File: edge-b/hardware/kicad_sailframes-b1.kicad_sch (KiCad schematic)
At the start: 49 parts, among them J2 JST_PH_BAT, J3 U.FL, U1 LC29HEAMD, U2 TP4056, U3 MT3608

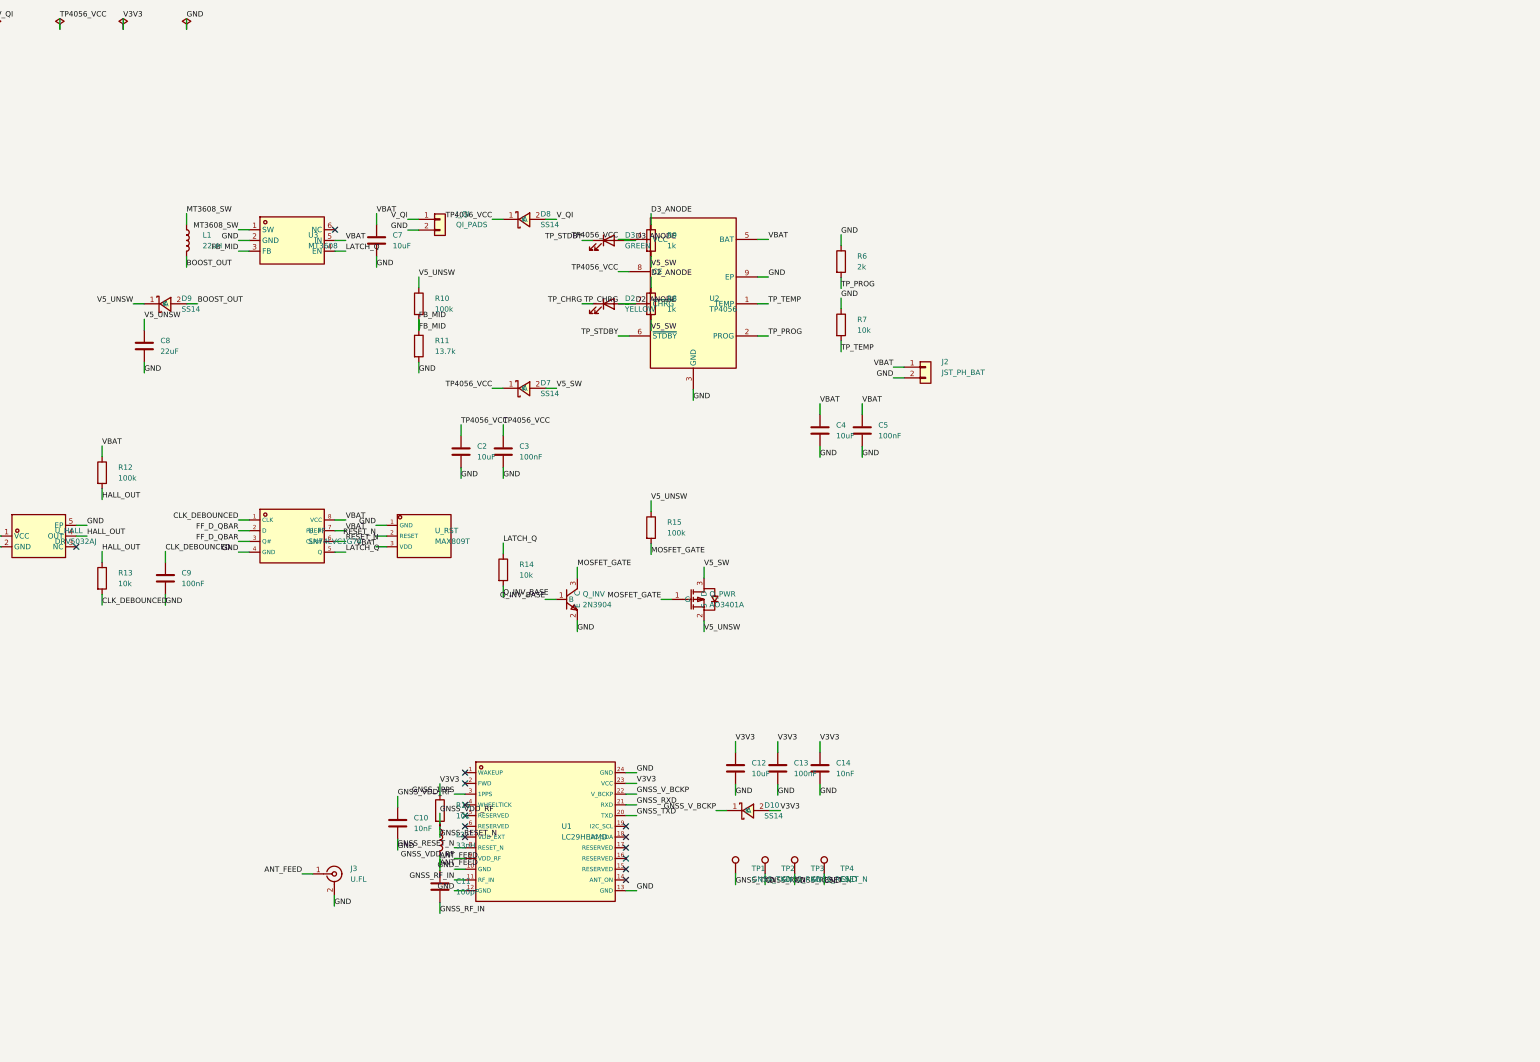
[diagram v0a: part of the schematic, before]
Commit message: B1 schematic Sections 4+5+6+7+9: ESP32, BNO085, TFT, microSD, LEDs
29 new components completing the schematic capture:
- Section 4: U4 ESP32 DevKit V1 socket (30-pin) with full GPIO mapping
  per B1_PIN_MAP.md. 6 pins marked no_connect (EN/VP/D12/D15/RX0/TX0 —
  reserved, strapping, or USB-handled).
- Section 5: J8 BNO085 9-pin socket + R21/R22 4.7K I2C pull-ups to V3V3.
  5 breakout pins marked no_connect (3Vo/INT/RST/P0/P1 — N/C per spec
  line 866).
- Section 6: J9 Hosyond 3.5" ST7796U TFT (14-pin) socket. 6 unused pins
  marked no_connect (touch + SD interface, neither used in B1).
- Section 7: J5 microSD socket (7-pin SPI) + R23-R27 10K pull-ups on
  CS/MOSI/MISO/SCK/CD + C15/C16 (10uF + 100nF) VCC decoupling.
- Section 9: D1 (Blue, Qi present, V_QI via R20 470Ω), D4 (Red,
  heartbeat, GPIO33 via R17 220Ω), D5 (White, GPS fix, GPIO32 via R18),
  D6 (Cyan, SD activity, GPIO26 via R19). All active-LOW from ESP32 side.

Paper size changed A4 → A3 (420×297 mm). Section 3 was off the A4 page
bottom; A3 gives room for all 9 sections + PWR_FLAGs without overlap.

New lib_symbols added:
- ESP32_DEVKITV1:ESP32_DEVKITV1 (30 pins, custom)
- Hosyond_TFT_ST7796U:Hosyond_3.5_ST7796U (14 pins, custom)
- Connector_Generic:Conn_01x07 (microSD)
- Connector_Generic:Conn_01x09 (BNO085)

Every previously-dangling label from Sections 1-3+10 now has its second
reference:
- GNSS_TXD/RXD: 3 each (LC29HEAMD + TP1/TP2 + ESP32 RX2/TX2)
- GNSS_1PPS: 2 (LC29HEAMD + ESP32 VN)
- I2C_SDA/SCL: 3 each (ESP32 + BNO085 + pull-up)
- HSPI_*: 3 each (ESP32 + microSD + pull-up)
- VSPI_SCK/MOSI: 2 each (ESP32 + TFT)
- TFT_BL/CS/RST/DC: 2 each (ESP32 + TFT)
- LED_HB_N/GPS_N/SD_N: 2 each (ESP32 + LED cathode)
- VBAT_DIV: 4 (ESP32 D34 + R1/R2/C1 battery monitor)
- V_QI: 4 (Qi pads + SS14 + D1/R20 indicator)

ERC after batch B (kicad-cli):
- pin_not_connected:    0
- unconnected_endpoint: 0
- isolated_pin_label:   1 (LATCH_Q_RB — needs spec line 837's 10K +
                            3.3V clamp diode leve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
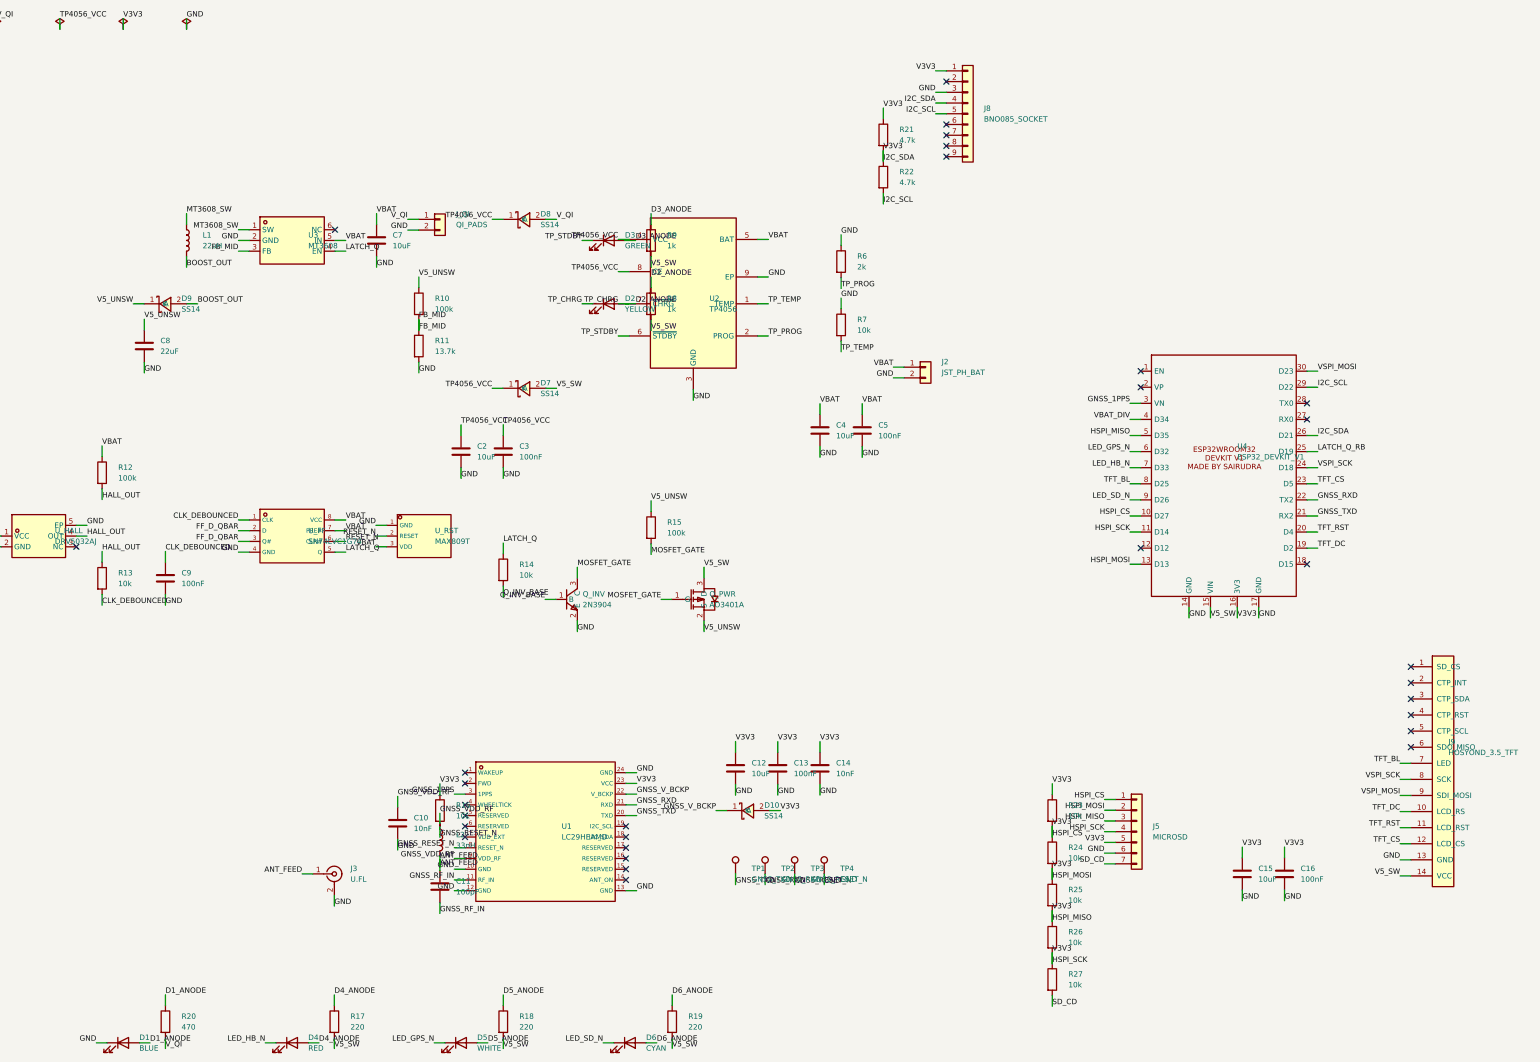
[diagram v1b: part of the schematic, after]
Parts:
- added C15: 10uF, Capacitor_SMD:C_0603_1608Metric, symbol Device:C
- added C16: 100nF, Capacitor_SMD:C_0603_1608Metric, symbol Device:C
- added D1: BLUE, LED_SMD:LED_0603_1608Metric, symbol Device:LED
- added D4: RED, LED_SMD:LED_0603_1608Metric, symbol Device:LED
- added D5: WHITE, LED_SMD:LED_0603_1608Metric, symbol Device:LED
- added D6: CYAN, LED_SMD:LED_0603_1608Metric, symbol Device:LED
- added J5: MICROSD, Connector_Card:microSD_HC_Hirose_DM3D-SF, symbol Connector_Generic:Conn_01x07
- added J8: BNO085_SOCKET, Connector_PinHeader_2.54mm:PinHeader_1x09_P2.54mm_Vertical, symbol Connector_Generic:Conn_01x09
- added J9: HOSYOND_3.5_TFT, Connector_PinHeader_2.54mm:PinHeader_2x08_P2.54mm_Vertical, symbol Hosyond_TFT_ST7796U:Hosyond_3.5_ST7796U
- added R17, R18, R19: 220, Resistor_SMD:R_0603_1608Metric, symbol Device:R
- added R20: 470, Resistor_SMD:R_0603_1608Metric, symbol Device:R
- added R21, R22: 4.7k, Resistor_SMD:R_0603_1608Metric, symbol Device:R
- added R23, R24, R25, R26, R27: 10k, Resistor_SMD:R_0603_1608Metric, symbol Device:R
- added U4: ESP32_DEVKIT_V1, Module:ESP32-DevKitC-V1, symbol ESP32_DEVKITV1:ESP32_DEVKITV1
- D2, D3: footprint LED_SMD:LED_0805_2012Metric -> LED_SMD:LED_0603_1608Metric
- L1: footprint Inductor_SMD:L_Bourns_SRR4528 -> Inductor_SMD:L_0805_2012Metric
- U_FF: footprint Package_SO:SM8 -> Package_SO:VSSOP-8_3.0x3.0mm_P0.65mm
- U_HALL: footprint Package_DFN_QFN:X2SON-4_1x1mm_P0.5mm -> Package_DFN_QFN:X2SON-4_1.0x1.0mm_P0.5mm
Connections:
- net GND: now also C15.2, C16.2, D1.1 (K), J5.6 (Pin_6), J8.3 (Pin_3), J9.13 (GND), U4.14 (GND), U4.17 (GND)
- net GNSS_1PPS: now also U4.3 (VN)
- net GNSS_RXD: now also U4.22 (TX2)
- net GNSS_TXD: now also U4.21 (RX2)
- net V5_SW: now also J9.14 (VCC), R17.2, R18.2, R19.2, U4.15 (VIN)
- net VBAT_DIV: now also U4.4 (D34)
- net V_QI: now also R20.2
- net V3V3 renamed HSPI_CS
- net HSPI_CS: now also C15.1, C16.1, J5.1 (Pin_1), J5.2 (Pin_2), J5.3 (Pin_3), J5.4 (Pin_4), J5.5 (Pin_5), J8.1 (Pin_1), J8.4 (Pin_4), R21.1, R21.2, R22.1, R23.1, R23.2, R24.1, R24.2, R25.1, R25.2, R26.1, R26.2, R27.1, U4.10 (D27), U4.11 (D14), U4.13 (D13), U4.16 (3V3), U4.26 (D21), U4.5 (D35)
- new net D1_ANODE: D1.2 (A), R20.1
- new net D4_ANODE: D4.2 (A), R17.1
- new net D5_ANODE: D5.2 (A), R18.1
- new net D6_ANODE: D6.2 (A), R19.1
- new net I2C_SCL: J8.5 (Pin_5), R22.2, U4.29 (D22)
- new net LATCH_Q_RB: U4.25 (D19)
- new net LED_GPS_N: D5.1 (K), U4.6 (D32)
- new net LED_HB_N: D4.1 (K), U4.7 (D33)
- new net LED_SD_N: D6.1 (K), U4.9 (D26)
- new net SD_CD: J5.7 (Pin_7), R27.2
- new net TFT_BL: J9.7 (LED), U4.8 (D25)
- new net TFT_CS: J9.12 (LCD_CS), U4.23 (D5)
- new net TFT_DC: J9.10 (LCD_RS), U4.19 (D2)
- new net TFT_RST: J9.11 (LCD_RST), U4.20 (D4)
- new net VSPI_MOSI: J9.9 (SDI_MOSI), U4.30 (D23)
- new net VSPI_SCK: J9.8 (SCK), U4.24 (D18)
- no-connect marks 14 -> 31

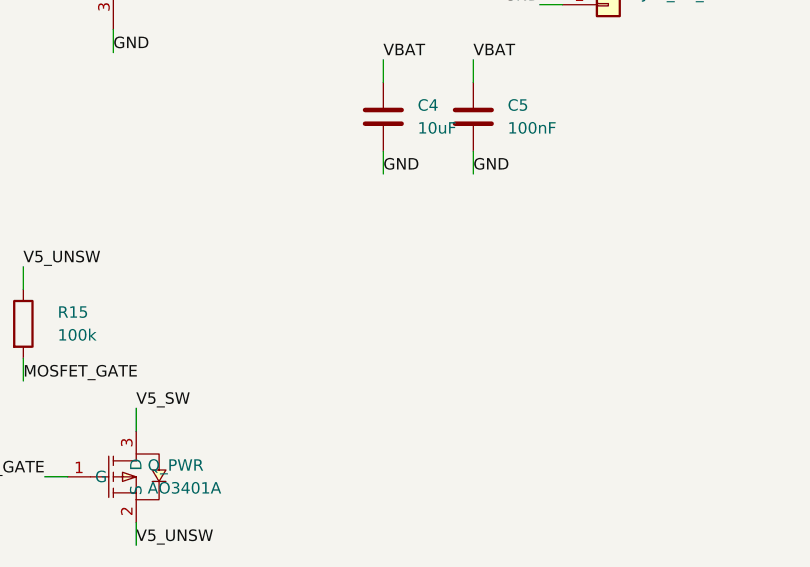
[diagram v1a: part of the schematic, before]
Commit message: B1 schematic: LATCH_Q_RB level shifter (Section 10 supplement)
Per spec line 837: ESP32 GPIO19 reads back the 74LVC1G74 Q output (up to
4.2 V from VBAT-powered FF). GPIO19 is 3.3 V tolerant, so the FF output
must be voltage-protected before connecting.

Adding 2 components:
- R28 10 KΩ in series between LATCH_Q (FF Q output, 4.2 V max) and
  LATCH_Q_RB (ESP32 GPIO19 input)
- D11 SS14 Schottky clamp diode, anode at LATCH_Q_RB, cathode at V3V3.
  When LATCH_Q_RB tries to exceed V3V3 + 0.3 V, D11 conducts and clamps
  the voltage to V3V3. The 10 KΩ series limits the clamp current to
  (4.2 - 3.6) / 10K = 60 µA, well within both the Schottky and the
  ESP32 GPIO ESD diode ratings.

Net resolution after this change:
- LATCH_Q: 4 labels (U_FF.Q + R14 + MT3608.EN + R28.1) — the critical
  double-gating signal now triple-fanout
- LATCH_Q_RB: 2 labels (R28.2 + ESP32.D19) — was the last isolated net

ERC after this commit (kicad-cli):
- pin_not_connected:    0
- unconnected_endpoint: 0
- isolated_pin_label:   0  ✓ schematic electrically complete
- pin_to_pin:          54 (easyeda2kicad cosmetic)
- footprint_link:       5 (footprint name cleanup)
- endpoint_off_grid:  289 (cosmetic)

Schematic capture done. Remaining work to ship: footprint assignment
verification, PCB layout (placement + routing + DRC).

Co-Authored-By: Claude Opus 4.7 (1M context) <noreply@anthropic.com>
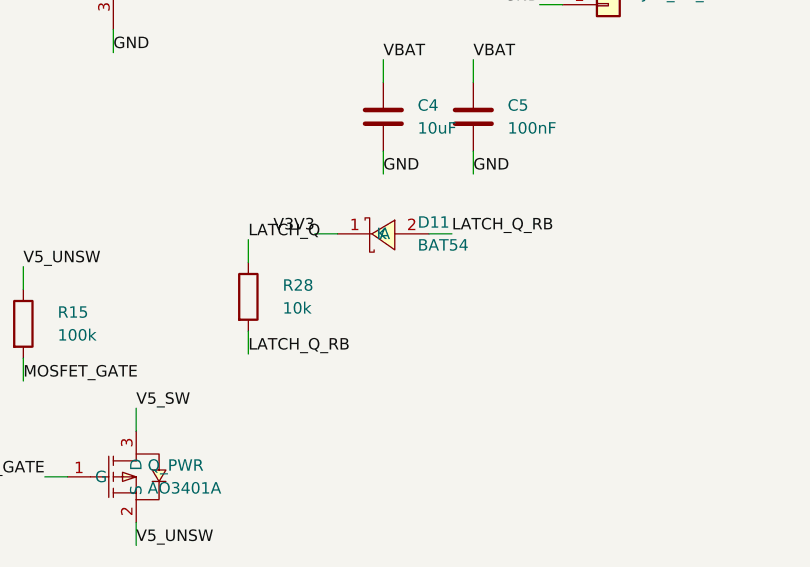
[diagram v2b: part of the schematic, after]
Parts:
- added D11: BAT54, Diode_SMD:D_SOD-323, symbol B1_SS14:SS14
- added R28: 10k, Resistor_SMD:R_0603_1608Metric, symbol Device:R
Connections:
- net HSPI_CS: now also D11.1 (K)
- net LATCH_Q: now also R28.1
- net LATCH_Q_RB: now also D11.2 (A), R28.2
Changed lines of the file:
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@@
+		)
+	)
+	(symbol
+		(lib_id "Device:R")
+		(at 250 145 0)
+		(unit 1)
+		(body_style 1)
+		(exclude_from_sim no)
+		(in_bom yes)
+		(on_board yes)
+		(in_pos_files yes)
+		(dnp no)
+		(fields_autoplaced yes)
+		(property "Reference" "R28"
+			(at 253.81 143.73 0)
+			(show_name no) (do_not_autoplace no)
+			(effects (font (size 1.27 1.27)) (justify left))
+		)
+		(property "Value" "10k"
+			(at 253.81 146.27 0)
+			(show_name no) (do_not_autoplace no)
+			(effects (font (size 1.27 1.27)) (justify left))
+		)
+		(property "Footprint" "Resistor_SMD:R_0603_1608Metric"
+			(at 250 145 0)
+			(hide yes) (show_name no) (do_not_autoplace no)
+			(effects (font (size 1.27 1.27)))
+		)
+		(property "Datasheet" "" (at 250 145 0) (hide yes) (show_name no) (do_not_autoplace no) (effects (font (size 1.27 1.27))))
+		(property "Description" "" (at 250 145 0) (hide yes) (show_name no) (do_not_autoplace no) (effects (font (size 1.27 1.27))))
+		(pin "1")
+		(pin "2")
+		(instances
+			(project "kicad_sailframes-b1"
+				(path "/55a15901-2456-4981-9aec-e05748aa87b1"
+					(reference "R28")
+					(unit 1)
+				)
+			)
+		)
+	)
+	(symbol
+		(lib_id "B1_SS14:SS14")
+		(at 265 138 0)
+		(unit 1)
+		(body_style 1)
+		(exclude_from_sim no)
+		(in_bom yes)
+		(on_board yes)
+		(in_pos_files yes)
+		(dnp no)
+		(fields_autoplaced yes)
+		(property "Reference" "D11"
+			(at 268.81 136.73 0)
+			(show_name no) (do_not_autoplace no)
+			(effects (font (size 1.27 1.27)) (justify left))
+		)
+		(property "Value" "BAT54"
+			(at 268.81 139.27 0)
+			(show_name no) (do_not_autoplace no)
+			(effects (font (size 1.27 1.27)) (justify left))
+		)
+		(property "Footprint" "Diode_SMD:D_SOD-323"
+			(at 265 138 0)
+			(hide yes) (show_name no) (do_not_autoplace no)
+			(effects (font (size 1.27 1.27)))
+		)
+		(property "Datasheet" "" (at 265 138 0) (hide yes) (show_name no) (do_not_autoplace no) (effects (font (size 1.27 1.27))))
+		(property "Description" "" (at 265 138 0) (hide yes) (show_name no) (do_not_autoplace no) (effects (font (size 1.27 1.27))))
+		(pin "1")
+		(pin "2")
+		(instances
+			(project "kicad_sailframes-b1"
+				(path "/55a15901-2456-4981-9aec-e05748aa87b1"
+					(reference "D11")
+					(unit 1)
+				)
+			)
 		)
 	)
@@
 		(effects (font (size 1.27 1.27)) (justify left bottom))
 	)
+	(wire
+		(pts (xy 250.0 141.19) (xy 250.0 138.65))
+		(stroke (width 0) (type default))
+	)
+	(label "LATCH_Q"
+		(at 250.0 138.65 0)
+		(effects (font (size 1.27 1.27)) (justify left bottom))
+	)
+	(wire
+		(pts (xy 250.0 148.81) (xy 250.0 151.35))
+		(stroke (width 0) (type default))
+	)
+	(label "LATCH_Q_RB"
+		(at 250.0 151.35 0)
+		(effects (font (size 1.27 1.27)) (justify left bottom))
+	)
+	(wire
+		(pts (xy 259.92 138.0) (xy 257.38 138.0))
+		(stroke (width 0) (type default))
+	)
+	(label "V3V3"
+		(at 257.38 138.0 0)
+		(effects (font (size 1.27 1.27)) (justify right bottom))
+	)
+	(wire
+		(pts (xy 270.08 138.0) (xy 272.62 138.0))
+		(stroke (width 0) (type default))
+	)
+	(label "LATCH_Q_RB"
+		(at 272.62 138.0 0)
+		(effects (font (size 1.27 1.27)) (justify left bottom))
+	)

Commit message: B1 schematic: footprint reference cleanup (5 link warnings → 0)
ERC was flagging 5 components whose Footprint field pointed at library
items that don't exist verbatim in KiCad's standard footprint libraries.
Resolved each by either (a) picking the actual KiCad standard name or
(b) pointing at the project-local footprint that ships in B1's libs.

Changes:
- L1 22uH:        Inductor_SMD:L_0805_2012Metric (too small for 22uH/1A)
                  → Inductor_SMD:L_Bourns_SRN6045TA (6x6mm shielded,
                    realistic for the part value)
- U_HALL:         Package_DFN_QFN:X2SON-4_1.0x1.0mm_P0.5mm (NX)
                  → B1_DRV5032AJ:X2SON-4_L1.1-W1.4-P0.50-BR-EP
                    (the easyeda2kicad-generated footprint with EP)
- U_FF:           Package_SO:VSSOP-8_3.0x3.0mm_P0.65mm (NX)
                  → B1_JLC:SM8_L3.0-W2.8-P0.65-LS4.0-BL
                    (JLC2KiCadLib SM8/SOT-23-8 footprint — spec line 102
                    mandates JLC2KiCadLib output for this part)
- U1 LC29HEAMD:   Package_LCC:LCC-24_4x4mm_P0.5mm (NX, also wrong
                  dimensions; real package is 16x12.2mm)
                  → B1_JLC:GPSM-SMD_24P-L16.0-W12.2-P1.10-TL
                    (JLC2KiCadLib actual LCC-24 footprint — per spec
                    line 102 the JLC2KiCadLib version is authoritative)
- J2 JST battery: Connector_JST:JST_PH_S2B-PH-K_1x02_P2.00mm_Vertical
                  (S2B is the cable-side connector; PCB needs B2B)
                  → Connector_JST:JST_PH_B2B-PH-K_1x02_P2.00mm_Vertical
- J9 TFT:         Connector_PinHeader_2.54mm:PinHeader_2x08_P2.54mm_Vertical
                  (Hosyond_3.5_ST7796U symbol is 14-pin single row)
                  → Connector_PinHeader_2.54mm:PinHeader_1x14_P2.54mm_Vertical
- U4 ESP32:       Module:ESP32-DevKitC-V1 (NX in KiCad standard libs)
                  → b1_Library:ESP32DEVIKITV1 (project-local footprint
                    that already ships in b1.pretty/)

ERC after cleanup:
- pin_not_connected:    0 (unc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
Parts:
- J2: footprint Connector_JST:JST_PH_S2B-PH-K_1x02_P2.00mm_Vertical -> Connector_JST:JST_PH_B2B-PH-K_1x02_P2.00mm_Vertical
- J9: footprint Connector_PinHeader_2.54mm:PinHeader_2x08_P2.54mm_Vertical -> Connector_PinHeader_2.54mm:PinHeader_1x14_P2.54mm_Vertical
- L1: footprint Inductor_SMD:L_0805_2012Metric -> Inductor_SMD:L_Bourns_SRN6045TA
- U1: footprint Package_LCC:LCC-24_4x4mm_P0.5mm -> B1_JLC:GPSM-SMD_24P-L16.0-W12.2-P1.10-TL
- U4: footprint Module:ESP32-DevKitC-V1 -> b1_Library:ESP32DEVIKITV1
- U_FF: footprint Package_SO:VSSOP-8_3.0x3.0mm_P0.65mm -> B1_JLC:SM8_L3.0-W2.8-P0.65-LS4.0-BL
- U_HALL: footprint Package_DFN_QFN:X2SON-4_1.0x1.0mm_P0.5mm -> B1_DRV5032AJ:X2SON-4_L1.1-W1.4-P0.50-BR-EP
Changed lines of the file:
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@@
 			(effects (font (size 1.27 1.27)) (justify left))
 		)
-		(property "Footprint" "Inductor_SMD:L_0805_2012Metric"
+		(property "Footprint" "Inductor_SMD:L_Bourns_SRN6045TA"
 			(at 115 80 0)
 			(hide yes) (show_name no) (do_not_autoplace no)
@@
 			(effects (font (size 1.27 1.27)) (justify left))
 		)
-		(property "Footprint" "Package_DFN_QFN:X2SON-4_1.0x1.0mm_P0.5mm"
+		(property "Footprint" "B1_DRV5032AJ:X2SON-4_L1.1-W1.4-P0.50-BR-EP"
 			(at 80 150 0)
 			(hide yes) (show_name no) (do_not_autoplace no)
@@
 			(effects (font (size 1.27 1.27)) (justify left))
 		)
-		(property "Footprint" "Package_SO:VSSOP-8_3.0x3.0mm_P0.65mm"
+		(property "Footprint" "B1_JLC:SM8_L3.0-W2.8-P0.65-LS4.0-BL"
 			(at 140 150 0)
 			(hide yes) (show_name no) (do_not_autoplace no)
@@
 			(effects (font (size 1.27 1.27)) (justify left))
 		)
-		(property "Footprint" "Connector_JST:JST_PH_S2B-PH-K_1x02_P2.00mm_Vertical"
+		(property "Footprint" "Connector_JST:JST_PH_B2B-PH-K_1x02_P2.00mm_Vertical"
 			(at 290 110 0)
 			(hide yes) (show_name no) (do_not_autoplace no)
@@
 			(effects (font (size 1.27 1.27)) (justify left))
 		)
-		(property "Footprint" "Package_LCC:LCC-24_4x4mm_P0.5mm"
+		(property "Footprint" "B1_JLC:GPSM-SMD_24P-L16.0-W12.2-P1.10-TL"
 			(at 200 220 0)
 			(hide yes) (show_name no) (do_not_autoplace no)
@@
 			(effects (font (size 1.27 1.27)) (justify left))
 		)
-		(property "Footprint" "Module:ESP32-DevKitC-V1"
+		(property "Footprint" "b1_Library:ESP32DEVIKITV1"
 			(at 360 130 0)
 			(hide yes) (show_name no) (do_not_autoplace no)
@@
 			(effects (font (size 1.27 1.27)) (justify left))
 		)
-		(property "Footprint" "Connector_PinHeader_2.54mm:PinHeader_2x08_P2.54mm_Vertical"
+		(property "Footprint" "Connector_PinHeader_2.54mm:PinHeader_1x14_P2.54mm_Vertical"
 			(at 410 200 0)
 			(hide yes) (show_name no) (do_not_autoplace no)
